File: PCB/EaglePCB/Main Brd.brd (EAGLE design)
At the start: 106.7 x 110.5 mm, 65 parts, among them J2 702461401, U1 ATWINC1500-MR210PB1952-T, U3 MSP430FR2355TDBTRDBT0038A_M, U6 ARJM11C7-114-BA-EW2

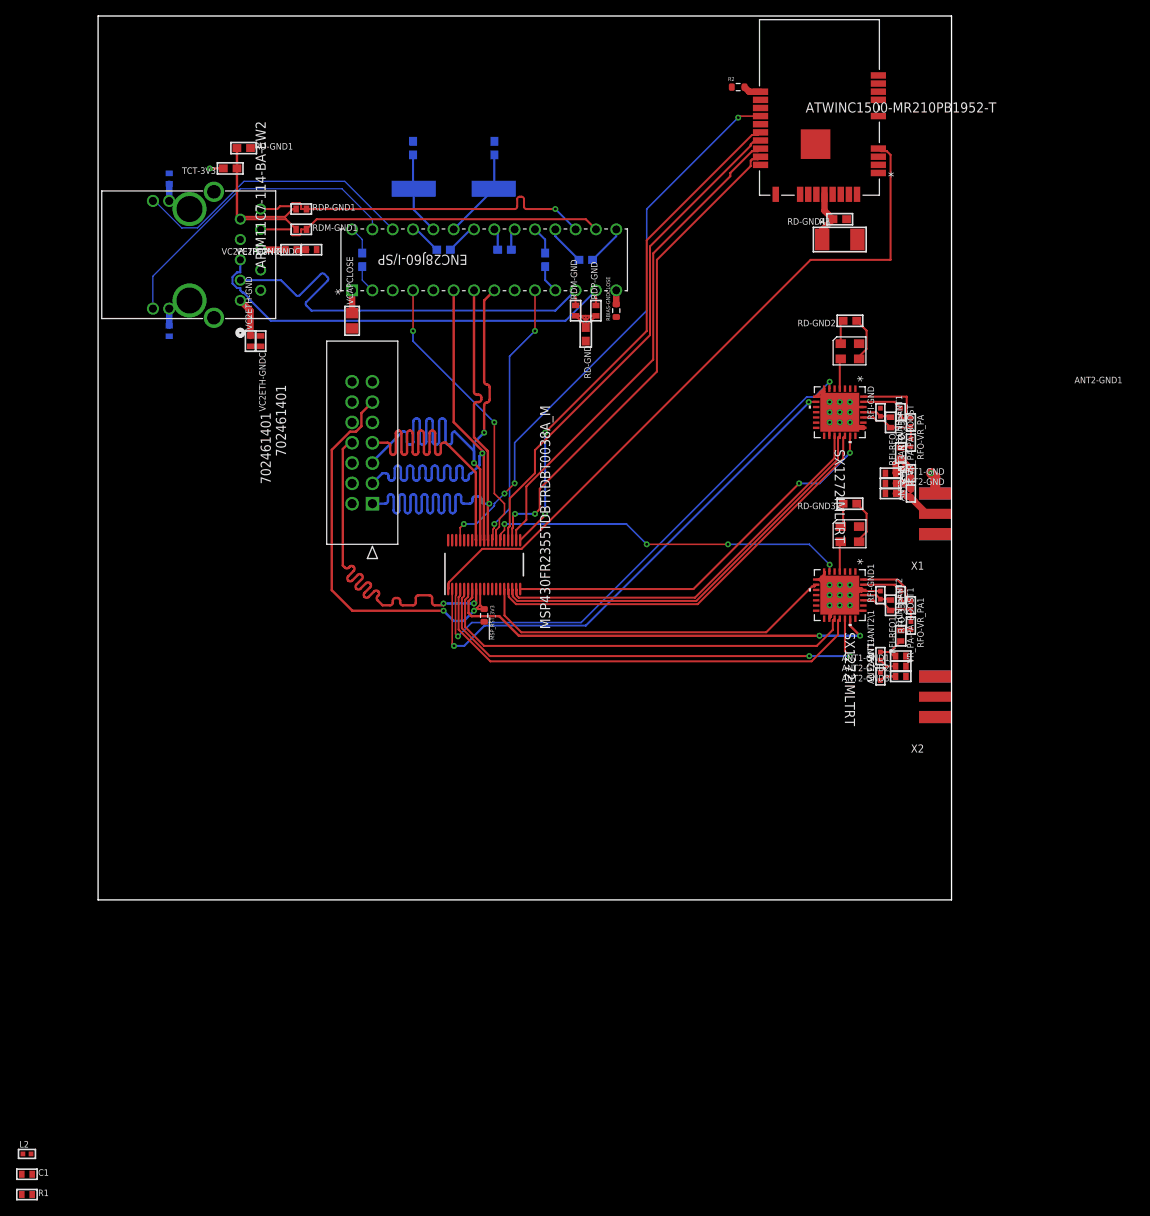
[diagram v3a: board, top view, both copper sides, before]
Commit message: added barrel connection
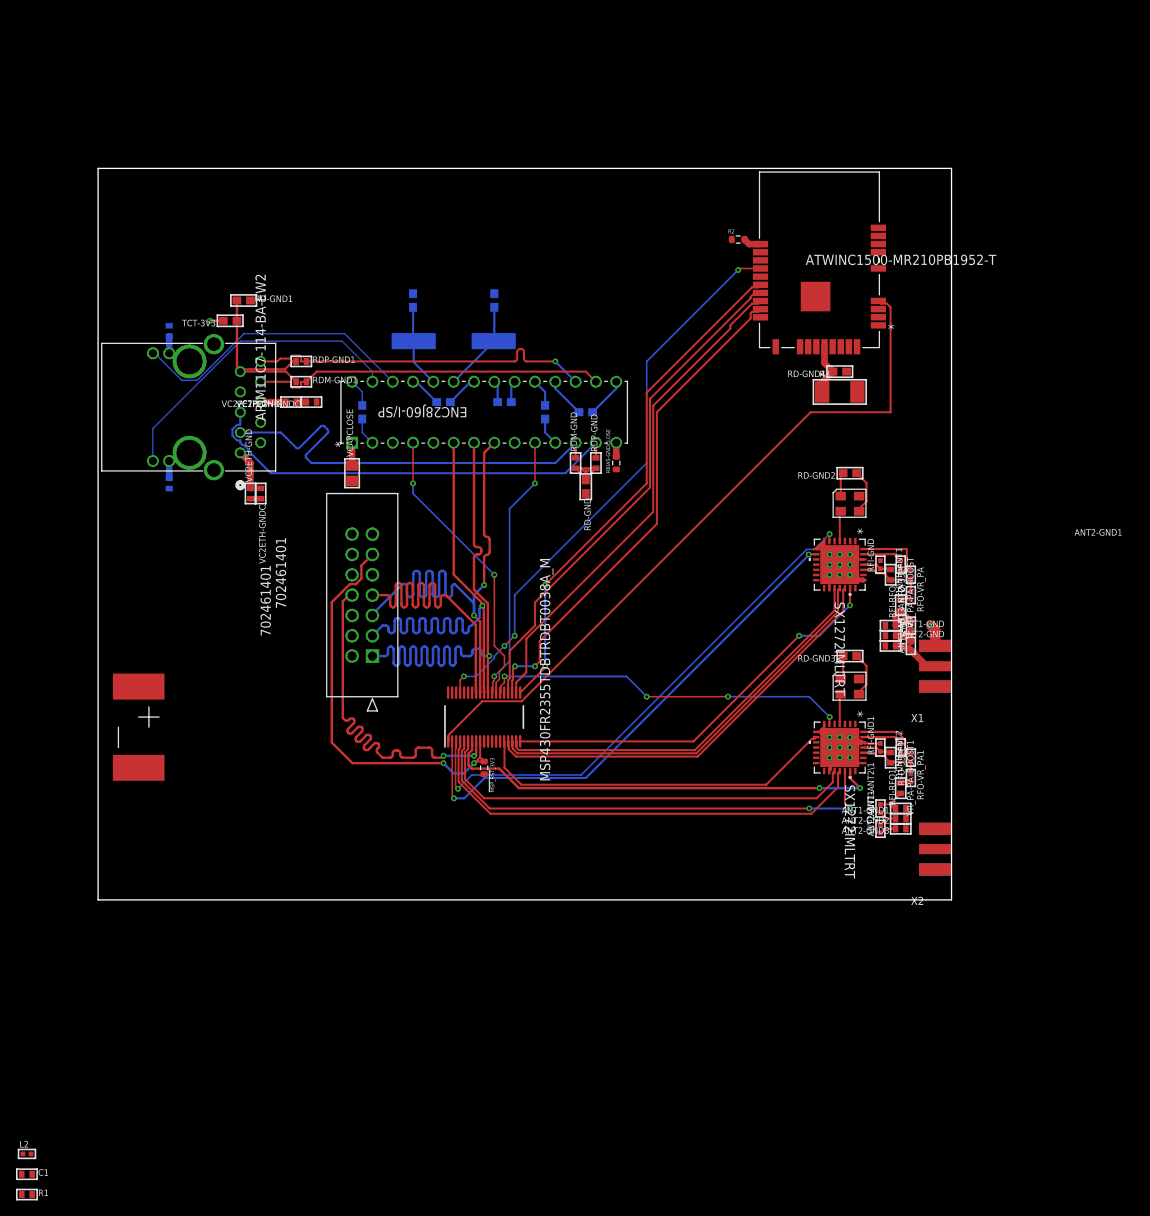
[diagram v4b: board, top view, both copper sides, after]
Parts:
- added U$7: BARREL_CONN_EXTERN, 473:BARREL_CONN_EXTERN
- moved U$2 19.1 mm to (44.5, 69.8)
- moved 10NH-ANT1 19.1 mm to (100.3, 36.8)
- moved 10NH-ANT2 19.1 mm to (100.3, 14.0)
- moved ANT1-ANT2\ 19.1 mm to (101.6, 34.3)
- moved ANT1-GND 19.1 mm to (99.1, 34.3)
- moved ETH 19.1 mm to (31.8, 57.1)
- moved LEDG 19.1 mm to (8.89, 52.1)
- moved LORA1 19.1 mm to (92.7, 41.9)
- moved RD-GND 19.1 mm to (61.0, 51.6)
- moved RFI-GND 19.1 mm to (97.8, 41.9)
- moved U6 19.1 mm to (17.8, 55.9)
- moved VC2PETH-GND 19.1 mm to (24.1, 62.2)
- moved VC2PETH-GNDC 19.1 mm to (26.7, 62.2)
- moved VR_PA-PA_BOOST 19.1 mm to (100.3, 41.9)
- moved VSS-VDD_ETH 19.1 mm to (33.0, 61.0)
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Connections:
- net 3V3: now also U$7.POS
- net GND: now also U$7.GND
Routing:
- net GND: track 87.9 -> 86.2 mm
- net !ETH_IRQ: track 36.9 -> 36.4 mm
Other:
- board size 106.7 x 110.5 mm -> 106.7 x 91.4 mm

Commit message: added keepout
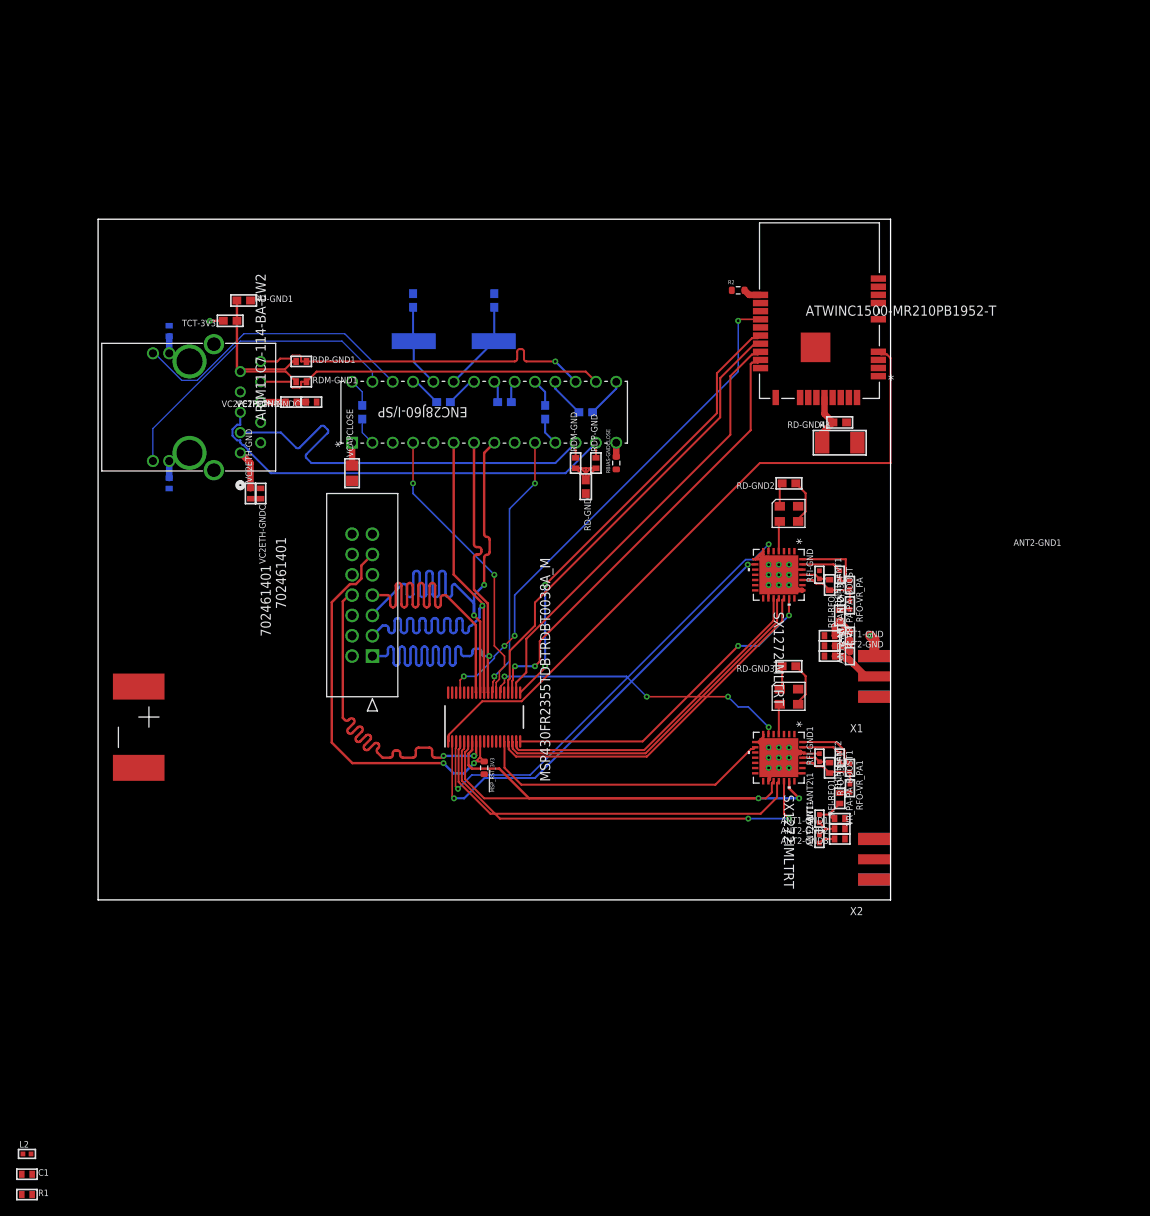
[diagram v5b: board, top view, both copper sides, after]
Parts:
- moved 10NH-ANT2 7.73 mm to (92.7, 12.7)
- moved ANT2-GND 7.73 mm to (91.4, 31.8)
- moved RD-GND2 7.73 mm to (86.4, 52.1)
- moved RFI-RFO 7.73 mm to (91.4, 39.4)
- moved TCXO1 7.73 mm to (86.4, 48.3)
- moved TCXO2 7.73 mm to (86.4, 25.4)
- moved 10NH-ANT1 7.73 mm to (92.7, 35.6)
- moved ANT1-ANT2\1 7.73 mm to (90.2, 10.2)
- moved ANT1-GND 7.73 mm to (91.4, 33.0)
- moved ANT1-GND1 7.73 mm to (92.7, 10.2)
- moved ANT2-ANT1 7.73 mm to (90.2, 7.62)
- moved ANT2-GND1 7.73 mm to (91.4, 30.5)
- moved ANT2-GND2 7.73 mm to (92.7, 8.89)
- moved ANT2-GND3 7.73 mm to (92.7, 7.62)
- moved RD-GND3 7.73 mm to (86.4, 29.2)
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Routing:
- net LORA2_SCK: track 54.2 -> 46.0 mm
- net LORA2_IRQ: track 45.6 -> 37.5 mm
- net LORA1_RST: track 66.6 -> 58.4 mm
- net LORA1_MISO: track 53.7 -> 45.5 mm
- net LORA1_CHIPSEL: track 50.4 -> 42.3 mm
- net LORA1_SCK: track 50.7 -> 42.6 mm
- net LORA2_MISO: track 57.7 -> 49.6 mm
- net LORA1_MOSI: track 52.2 -> 44.0 mm
- net LORA1_IRQ: track 65.2 -> 57.0 mm
- net LORA2_RST: track 45.9 -> 38.8 mm
- net LORA2_CHIPSEL: track 56.0 -> 48.9 mm
- net LORA2_MOSI: track 59.9 -> 52.8 mm
- net !ATC_IRQ: track 71.0 -> 64.6 mm
- net ATC_MOSI: track 63.9 -> 57.5 mm
- net ATC_SCK: track 62.7 -> 56.3 mm
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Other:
- board size 106.7 x 91.4 mm -> 99.1 x 85.1 mm
